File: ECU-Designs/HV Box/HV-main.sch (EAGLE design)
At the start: 67 parts, among them IC2 MCP6002SOIC, IC3 MCP6002SOIC

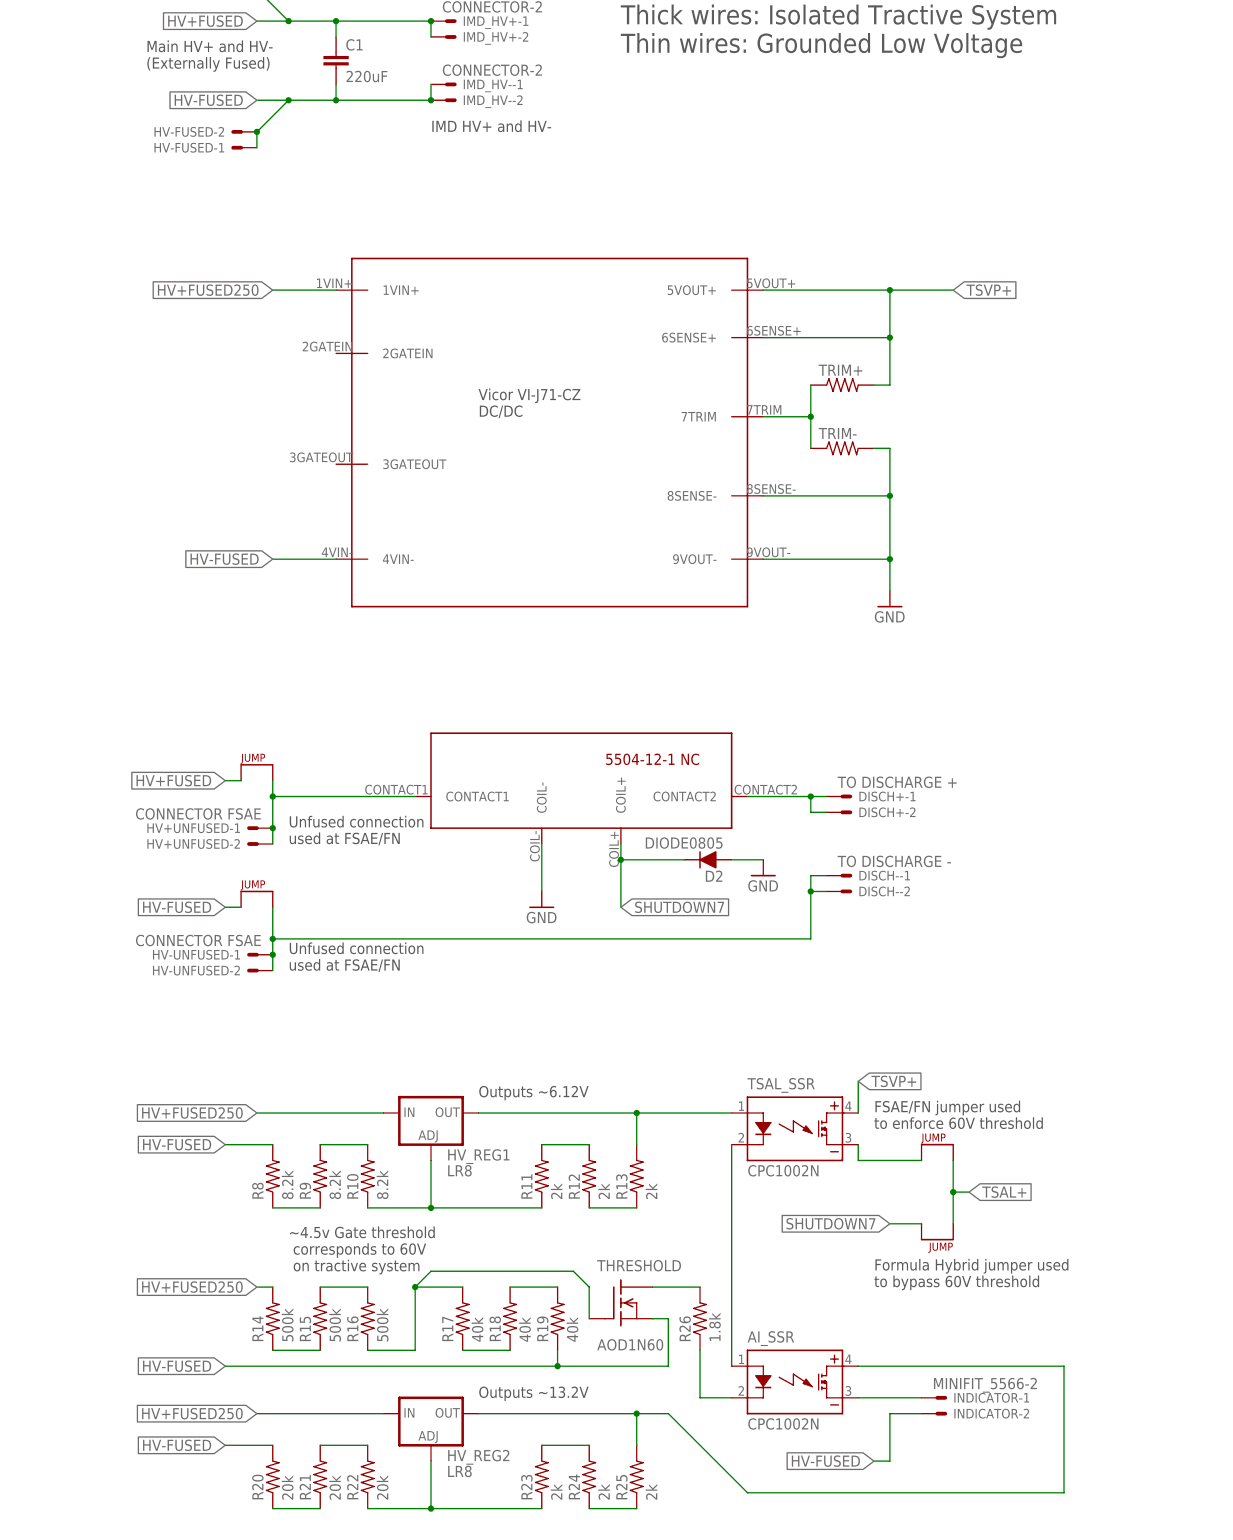
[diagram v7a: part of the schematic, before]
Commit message: Change HV brd to 5mm fuse, add second fuse, fix fuse sizing in library
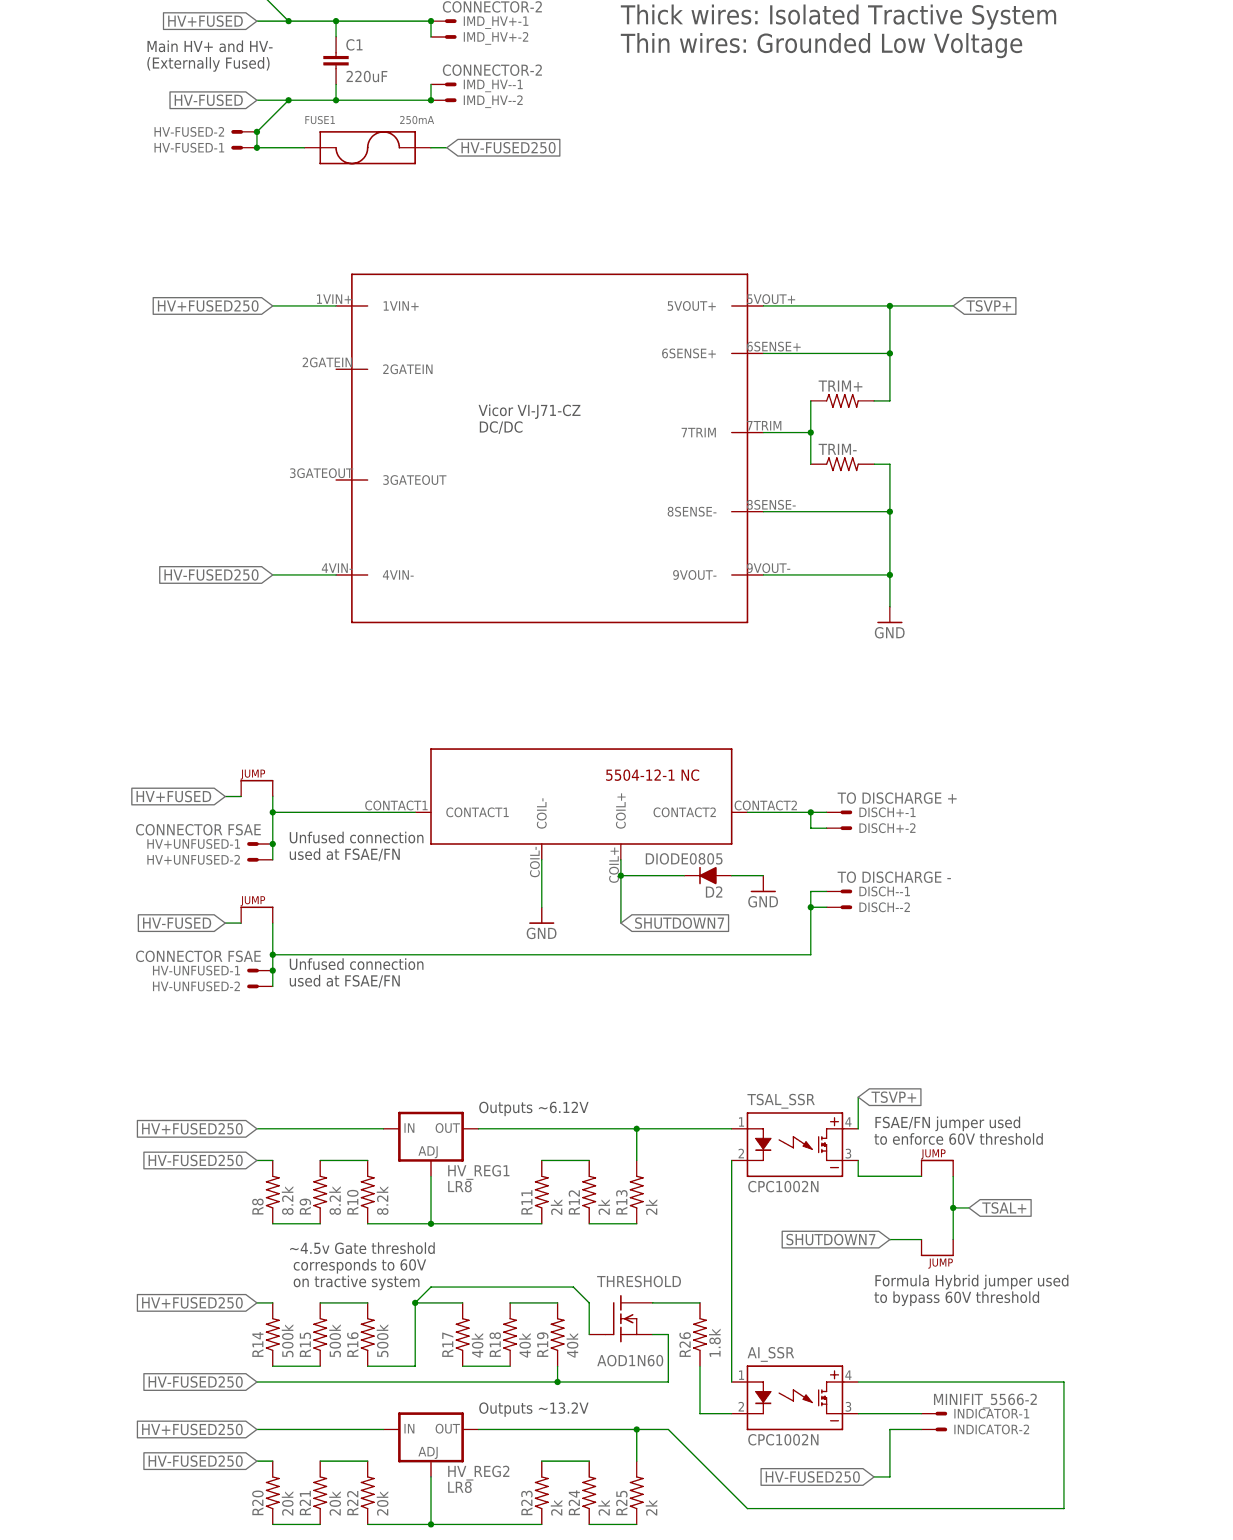
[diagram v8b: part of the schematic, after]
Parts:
- added FUSE1: 250mA, HyTechDevices:FUSE_5X20MM
- FUSE: device HyTechDevices:FUSE_MIDGET -> HyTechDevices:FUSE_5X20MM
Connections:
- new net HV-FUSED250: FUSE1.P2, INDICATOR-2.S, R19.1, R20.2, R8.2, THRESHOLD.S, U$5.4VIN-
- net HV-FUSED: now also FUSE1.P1; no longer INDICATOR-2.S, R19.1, R20.2, R8.2, THRESHOLD.S, U$5.4VIN-
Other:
- note removed: "IMD HV+ and HV-"
- moved on the sheet: AI_SSR, D2, DISCH+-1, DISCH+-2, DISCH--1, DISCH--2, HV+UNFUSED-1, HV+UNFUSED-2, HV-UNFUSED-1, HV-UNFUSED-2, HV_REG1, HV_REG2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
